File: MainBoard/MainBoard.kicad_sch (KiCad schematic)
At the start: 56 parts, among them J2 Non-Inverting Input, J3 Inverting Input, J4 Output, J5 InvertedOutput, J6 Inverting Input, J7 Non-Inverting Input, J8 Output, J9 InvertedOutput, Q16 BC557, Q32 BC557

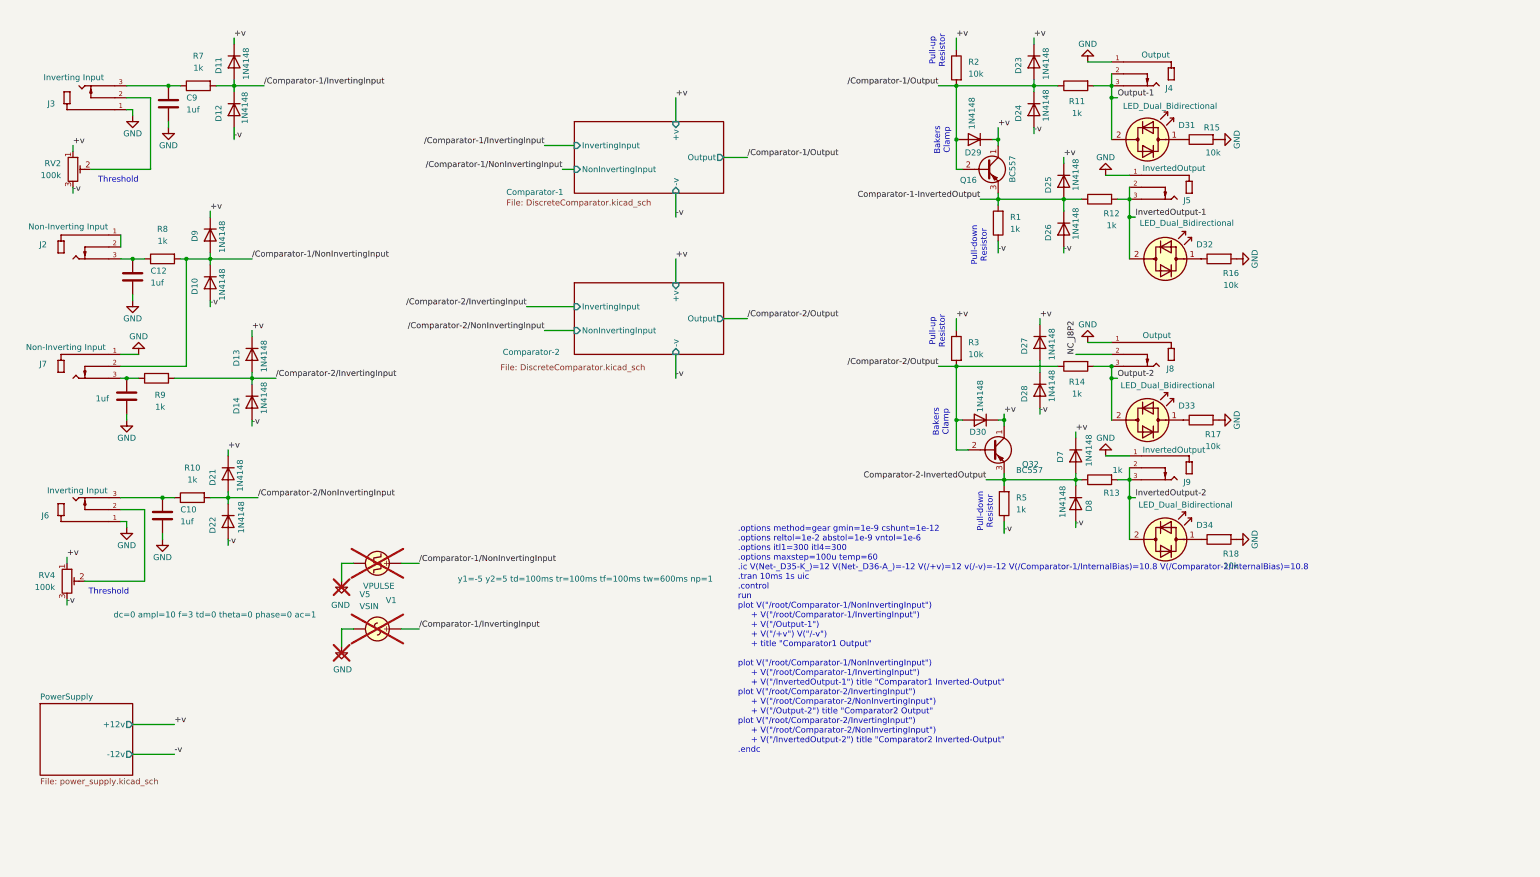
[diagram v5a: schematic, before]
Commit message: added additional voltage source for simulation
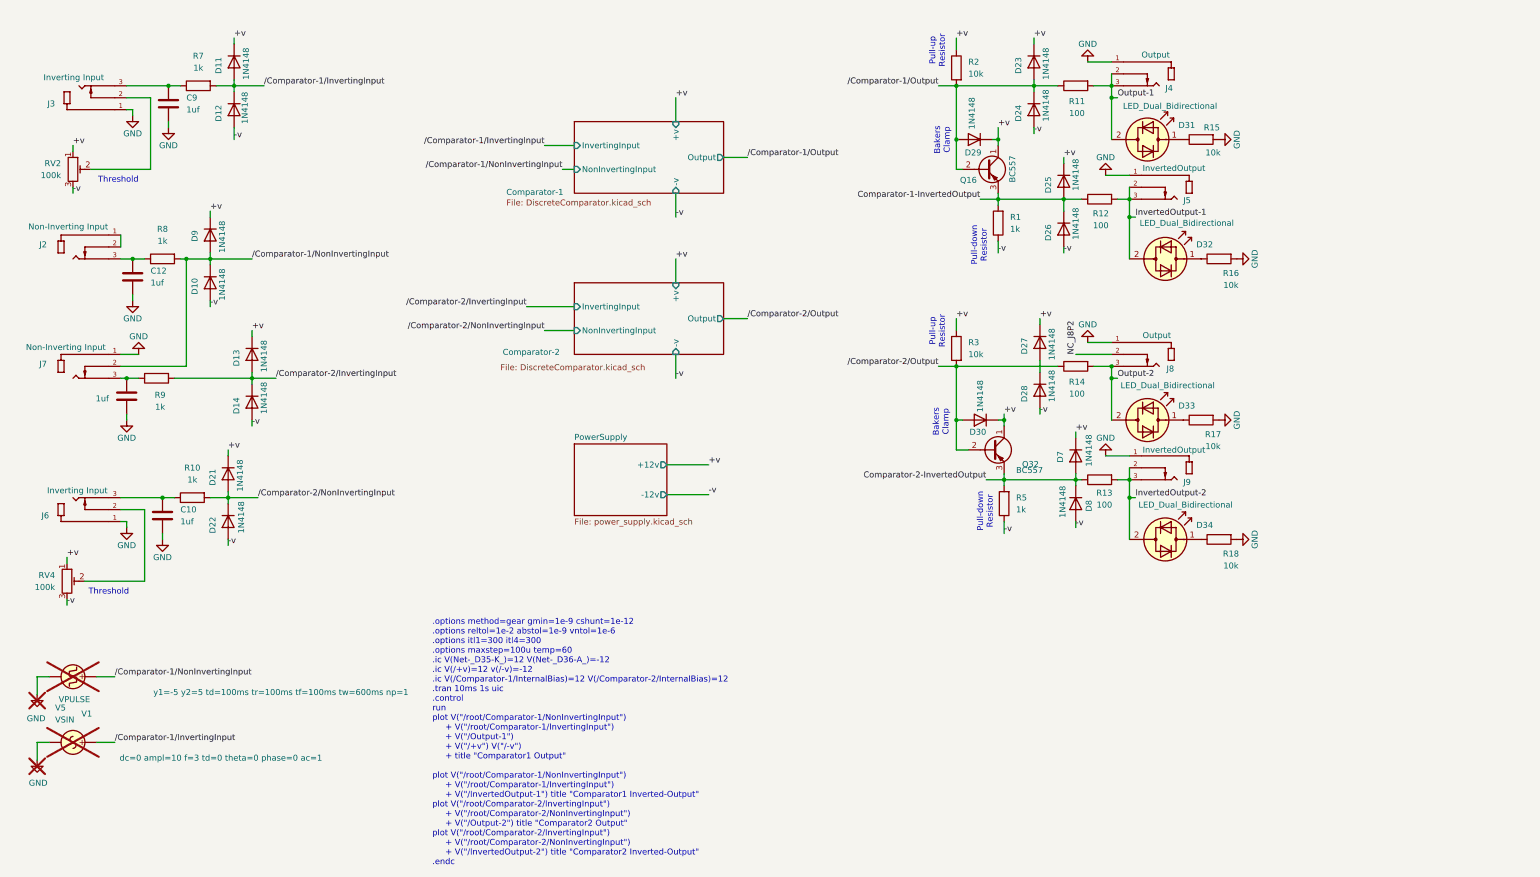
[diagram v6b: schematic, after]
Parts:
- R11, R12, R13, R14: value 1k -> 100
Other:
- note added: ".options method=gear gmin=1e-9 cshunt=1e-12 .options reltol=1e-2 abstol=1e-9 vntol=1e-6 .options itl1=300 itl4=300 .options maxstep=100u temp=60 .ic V(Net-_D35-K_)=12 V(Net-_D36-A_)=-12 .ic V(/+v)=12 v(/-v)=-12 .ic V(/Comparator-1/InternalBias)=12 V(/Comparator-2/InternalBias)=12 .tran 10ms 1s uic .control run plot V("/root/Comparator-1/NonInvertingInput") + V("/root/Comparator-1/InvertingInput")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"
- note removed: ".options method=gear gmin=1e-9 cshunt=1e-12 .options reltol=1e-2 abstol=1e-9 vntol=1e-6 .options itl1=300 itl4=300 .options maxstep=100u temp=60 .ic V(Net-_D35-K_)=12 V(Net-_D36-A_)=-12 V(/+v)=12 v(/-v)=-12 V(/Comparator-1/InternalBias)=10.8 V(/Comparator-2/InternalBias)=10.8 .tran 10ms 1s uic .control run plot V("/root/Comparator-1/NonInvertingInput") + V("/root/Comparator-1/InvertingInput") + V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"
- moved on the sheet: V1, V5
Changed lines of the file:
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@@
 		)
 	)
-	(text ".options method=gear gmin=1e-9 cshunt=1e-12 \n.options reltol=1e-2 abstol=1e-9 vntol=1e-6 \n.options itl1=300 itl4=300 \n.options maxstep=100u temp=60\n.ic V(Net-_D35-K_)=12 V(Net-_D36-A_)=-12 V(/+v)=12 v(/-v)=-12 V(/Comparator-1/InternalBias)=10.8 V(/Comparator-2/InternalBias)=10.8\n.tran 10ms 1s uic\n.control\nrun\nplot V(\"/root/Comparator-1/NonInvertingInput\") \n     + V(\"/root/Comparator-1/InvertingInput\") \n     + V(\"/Output-1\")\n     + V(\"/+v\") V(\"/-v\")\n     + title \"Comparator1 Output\" \n    \nplot V(\"/root/Comparator-1/NonInvertingInput\")\n     + V(\"/root/Comparator-1/InvertingInput\")\n     + V(\"/InvertedOutput-1\") title \"Comparator1 Inverted-Output\"\nplot V(\"/root/Comparator-2/InvertingInput\") \n     + V(\"/root/Comparator-2/NonInvertingInput\")   \n     + V(\"/Output-2\") title \"Comparator2 Output\" \nplot V(\"/root/Comparator-2/InvertingInput\")\n     + V(\"/root/Comparator-2/NonInvertingInput\") \n     + V(\"/InvertedOutput-2\") title \"Comparator2 Inverted-Output\"\n.endc"
+	(text ".options method=gear gmin=1e-9 cshunt=1e-12 \n.options reltol=1e-2 abstol=1e-9 vntol=1e-6 \n.options itl1=300 itl4=300 \n.options maxstep=100u temp=60\n.ic V(Net-_D35-K_)=12 V(Net-_D36-A_)=-12 \n.ic V(/+v)=12 v(/-v)=-12 \n.ic V(/Comparator-1/InternalBias)=12 V(/Comparator-2/InternalBias)=12\n.tran 10ms 1s uic\n.control\nrun\nplot V(\"/root/Comparator-1/NonInvertingInput\") \n     + V(\"/root/Comparator-1/InvertingInput\") \n     + V(\"/Output-1\")\n     + V(\"/+v\") V(\"/-v\")\n     + title \"Comparator1 Output\" \n    \nplot V(\"/root/Comparator-1/NonInvertingInput\")\n     + V(\"/root/Comparator-1/InvertingInput\")\n     + V(\"/InvertedOutput-1\") title \"Comparator1 Inverted-Output\"\nplot V(\"/root/Comparator-2/InvertingInput\") \n     + V(\"/root/Comparator-2/NonInvertingInput\")   \n     + V(\"/Output-2\") title \"Comparator2 Output\" \nplot V(\"/root/Comparator-2/InvertingInput\")\n     + V(\"/root/Comparator-2/NonInvertingInput\") \n     + V(\"/InvertedOutput-2\") title \"Comparator2 Inverted-Output\"\n.endc"
 		(exclude_from_sim no)
-		(at 170.688 147.066 0)
+		(at 105.664 168.91 0)
 		(effects
 			(font
@@
 	(wire
 		(pts
-			(xy 86.36 144.78) (xy 86.36 148.59)
+			(xy 21.59 168.91) (xy 21.59 172.72)
 		)
 		(stroke
@@
 	(wire
 		(pts
-			(xy 99.06 130.81) (xy 102.87 130.81)
+			(xy 34.29 154.94) (xy 38.1 154.94)
 		)
 		(stroke
@@
 	(wire
 		(pts
-			(xy 41.91 165.1) (xy 50.8 165.1)
+			(xy 155.575 109.855) (xy 164.465 109.855)
 		)
 		(stroke
@@
 	(wire
 		(pts
-			(xy 41.91 171.45) (xy 50.8 171.45)
+			(xy 155.575 116.205) (xy 164.465 116.205)
 		)
 		(stroke
@@
 	(wire
 		(pts
-			(xy 99.06 144.78) (xy 102.87 144.78)
+			(xy 34.29 168.91) (xy 38.1 168.91)
 		)
 		(stroke
@@
 	(wire
 		(pts
-			(xy 88.9 144.78) (xy 86.36 144.78)
+			(xy 24.13 168.91) (xy 21.59 168.91)
 		)
 		(stroke
@@
 	(wire
 		(pts
-			(xy 86.36 130.81) (xy 86.36 134.62)
+			(xy 21.59 154.94) (xy 21.59 158.75)
 		)
 		(stroke
@@
 	(wire
 		(pts
-			(xy 86.36 130.81) (xy 88.9 130.81)
+			(xy 21.59 154.94) (xy 24.13 154.94)
 		)
 		(stroke
@@
 	)
 	(label "+v"
-		(at 50.8 165.1 0)
+		(at 164.465 109.855 0)
 		(effects
 			(font
@@
 	)
 	(label "{slash}Comparator-1{slash}NonInvertingInput"
-		(at 102.87 130.81 0)
+		(at 38.1 154.94 0)
 		(effects
 			(font
@@
 	)
 	(label "-v"
-		(at 50.8 171.45 0)
+		(at 164.465 116.205 0)
 		(effects
 			(font
@@
 	)
 	(label "{slash}Comparator-1{slash}InvertingInput"
-		(at 102.87 144.78 0)
+		(at 38.1 168.91 0)
 		(effects
 			(font
@@
 	(symbol
 		(lib_id "power:GND")
-		(at 86.36 148.59 0)
+		(at 21.59 172.72 0)
 		(unit 1)
 		(exclude_from_sim no)
@@
 		(dnp yes)
 		(property "Reference" "#PWR07"
-			(at 86.36 154.94 0)
+			(at 21.59 179.07 0)
 			(effects
 				(font
@@
 		)
 		(property "Value" "GND"
-			(at 84.582 153.416 0)
+			(at 19.812 177.546 0)
 			(effects
 				(font
@@
 		)
 		(property "Footprint" ""
-			(at 86.36 148.59 0)
+			(at 21.59 172.72 0)
 			(effects
 				(font
@@
 		)
 		(property "Datasheet" ""
-			(at 86.36 148.59 0)
+			(at 21.59 172.72 0)
 			(effects
 				(font
@@
 		)
 		(property "Description" "Power symbol creates a global label with name \"GND\" , ground"
-			(at 86.36 148.59 0)
+			(at 21.59 172.72 0)
 			(effects
 				(font
@@
 	(symbol
 		(lib_id "Simulation_SPICE:VPULSE")
-		(at 93.98 130.81 270)
+		(at 29.21 154.94 270)
 		(mirror x)
 		(unit 1)
@@
 		(dnp yes)
 		(property "Reference" "V1"
-			(at 95.758 138.684 90)
+			(at 30.988 162.814 90)
 			(effects
 				(font
@@
 		)
 		(property "Value" "VPULSE"
-			(at 90.932 135.636 90)
+			(at 26.162 159.766 90)
 			(effects
 				(font
@@
 		)
 		(property "Footprint" ""
-			(at 93.98 130.81 0)
+			(at 29.21 154.94 0)
 			(effects
 				(font
@@
 		)
 		(property "Datasheet" "https://ngspice.sourceforge.io/docs/ngspice-html-manual/manual.xhtml#sec_Independent_Sources_for"
-			(at 93.98 130.81 0)
+			(at 29.21 154.94 0)
 			(effects
 				(font
@@
 		)
 		(property "Description" "Voltage source, pulse"
-			(at 93.98 130.81 0)
+			(at 29.21 154.94 0)
 			(effects
 				(font
@@
 		)
 		(property "Sim.Pins" "1=+ 2=-"
-			(at 93.98 130.81 0)
+			(at 29.21 154.94 0)
 			(effects
 				(font
@@
 		)
 		(property "Sim.Type" "PULSE"
-			(at 93.98 130.81 0)
+			(at 29.21 154.94 0)
 			(effects
 				(font
@@
 		)
 		(property "Sim.Device" "V"
-			(at 93.98 130.81 0)
+			(at 29.21 154.94 0)
 			(effects
 				(font
@@
 		)
 		(property "Sim.Params" "y1=-5 y2=5 td=100ms tr=100ms tf=100ms tw=600ms np=1"
-			(at 165.354 134.112 90)
+			(at 100.584 158.242 90)
 			(effects
 				(font
@@
 		(dnp no)
 		(property "Reference" "R13"
-			(at 250.19 115.824 90)
+			(at 248.666 115.824 90)
 			(effects
 				(font
@@
 			)
 		)
-		(property "Value" "1k"
-			(at 251.46 110.998 90)
+		(property "Value" "100"
+			(at 248.666 118.364 90)
 			(effects
 				(font
@@
 	(symbol
 		(lib_id "power:GND")
-		(at 86.36 134.62 0)
+		(at 21.59 158.75 0)
 		(mirror y)
 		(unit 1)
@@
 		(dnp yes)
 		(property "Reference" "#PWR02"
-			(at 86.36 140.97 0)
+			(at 21.59 165.1 0)
 			(effects
 				(font
@@
 		)
 		(property "Value" "GND"
-			(at 88.138 139.7 0)
+			(at 23.368 163.83 0)
 			(effects
 				(font
@@
 		)
 		(property "Footprint" ""
-			(at 86.36 134.62 0)
+			(at 21.59 158.75 0)
 			(effects
 				(font
@@
 		)
 		(property "Datasheet" ""
-			(at 86.36 134.62 0)
+			(at 21.59 158.75 0)
 			(effects
 				(font
@@
 		)
 		(property "Description" "Power symbol creates a global label with name \"GND\" , ground"
-			(at 86.36 134.62 0)
+			(at 21.59 158.75 0)
 			(effects
 				(font
@@
 			)
 		)
-		(property "Value" "1k"
+		(property "Value" "100"
 			(at 242.824 94.742 90)
 			(effects
@@
 	(symbol
 		(lib_id "Simulation_SPICE:VSIN")
-		(at 93.98 144.78 270)
+		(at 29.21 168.91 270)
 		(mirror x)
 		(unit 1)
@@
 		(dnp yes)
 		(property "Reference" "V5"
-			(at 90.17 137.414 90)
+			(at 25.4 161.544 90)
 			(effects
 				(font
@@
 		)
 		(property "Value" "VSIN"
-			(at 90.17 139.954 90)
+			(at 25.4 164.084 90)
 			(effects
 				(font
@@
 		)
 		(property "Footprint" ""
-			(at 93.98 144.78 0)
+			(at 29.21 168.91 0)
 			(effects
 				(font
@@
 		)
 		(property "Datasheet" "https://ngspice.sourceforge.io/docs/ngspice-html-manual/manual.xhtml#sec_Independent_Sources_for"
-			(at 93.98 144.78 0)
+			(at 29.21 168.91 0)
 			(effects
 				(font
@@
 		)
 		(property "Description" "Voltage source, sinusoidal"
-			(at 93.98 144.78 0)
+			(at 29.21 168.91 0)
 			(effects
 				(font
@@
 		)
 		(property "Sim.Pins" "1=+ 2=-"
-			(at 93.98 144.78 0)
+			(at 29.21 168.91 0)
 			(effects
 				(font
@@
 		)
 		(property "Sim.Params" "dc=0 ampl=10 f=3 td=0 theta=0 phase=0 ac=1"
-			(at 37.846 141.732 90)
+			(at 39.116 172.212 90)
 			(effects
 				(font
@@
 		)
 		(property "Sim.Type" "SIN"
-			(at 93.98 144.78 0)
+			(at 29.21 168.91 0)
 			(effects
 				(font
@@
 		)
 		(property "Sim.Device" "V"
-			(at 93.98 144.78 0)
+			(at 29.21 168.91 0)
 			(effects
 				(font
@@
 		(dnp no)
 		(property "Reference" "R12"
-			(at 250.19 56.388 90)
+			(at 247.904 56.388 90)
 			(effects
 				(font
@@
 			)
 		)
-		(property "Value" "1k"
-			(at 250.19 58.928 90)
+		(property "Value" "100"
+			(at 247.904 58.928 90)
 			(effects
 				(font
@@
 			)
 		)
-		(property "Value" "1k"
+		(property "Value" "100"
 			(at 242.824 35.052 90)
 			(effects
@@
 	)
 	(sheet
-		(at 22.225 160.655)
+		(at 135.89 105.41)
 		(size 19.685 15.24)
 		(exclude_from_sim no)
@@
 		)
 		(property "Sheetname" "PowerSupply"
-			(at 22.225 159.9434 0)
+			(at 135.89 104.6984 0)
 			(effects
 				(font
@@
 		)
 		(property "Sheetfile" "power_supply.kicad_sch"
-			(at 22.225 176.4796 0)
+			(at 135.89 121.2346 0)
 			(effects
 				(font
@@
 		)
 		(pin "+12v" output
-			(at 41.91 165.1 0)
+			(at 155.575 109.855 0)
 			(effects
 				(font
@@
 		)
 		(pin "-12v" output
-			(at 41.91 171.45 0)
+			(at 155.575 116.205 0)
 			(effects
 				(font
